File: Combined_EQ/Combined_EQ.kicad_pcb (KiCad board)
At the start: 2 copper layers, 152.3 x 105 mm, 1 part, among them J1 EDA 306

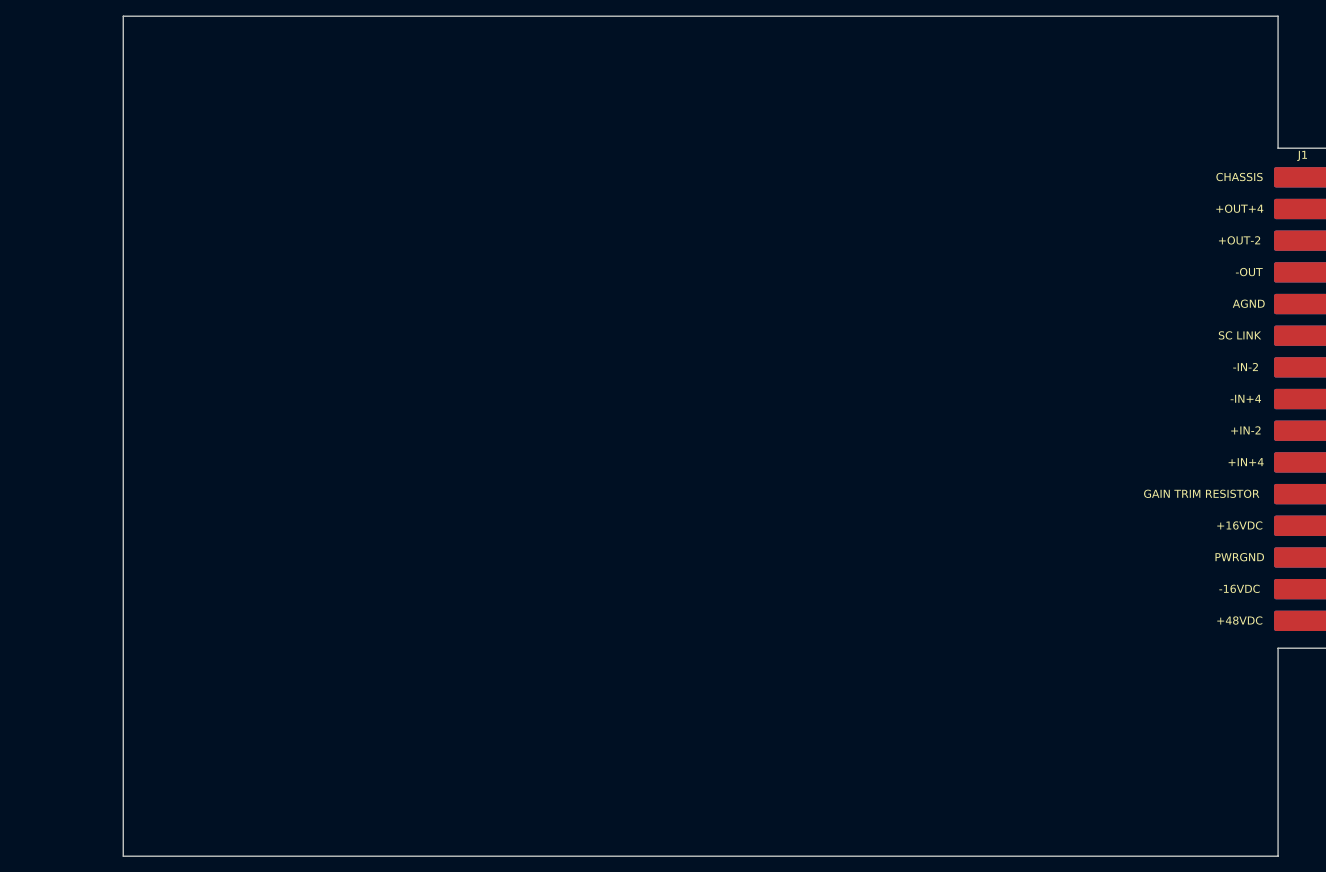
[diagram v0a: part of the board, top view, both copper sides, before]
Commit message: started on pcb
need to footprint for the capacitors
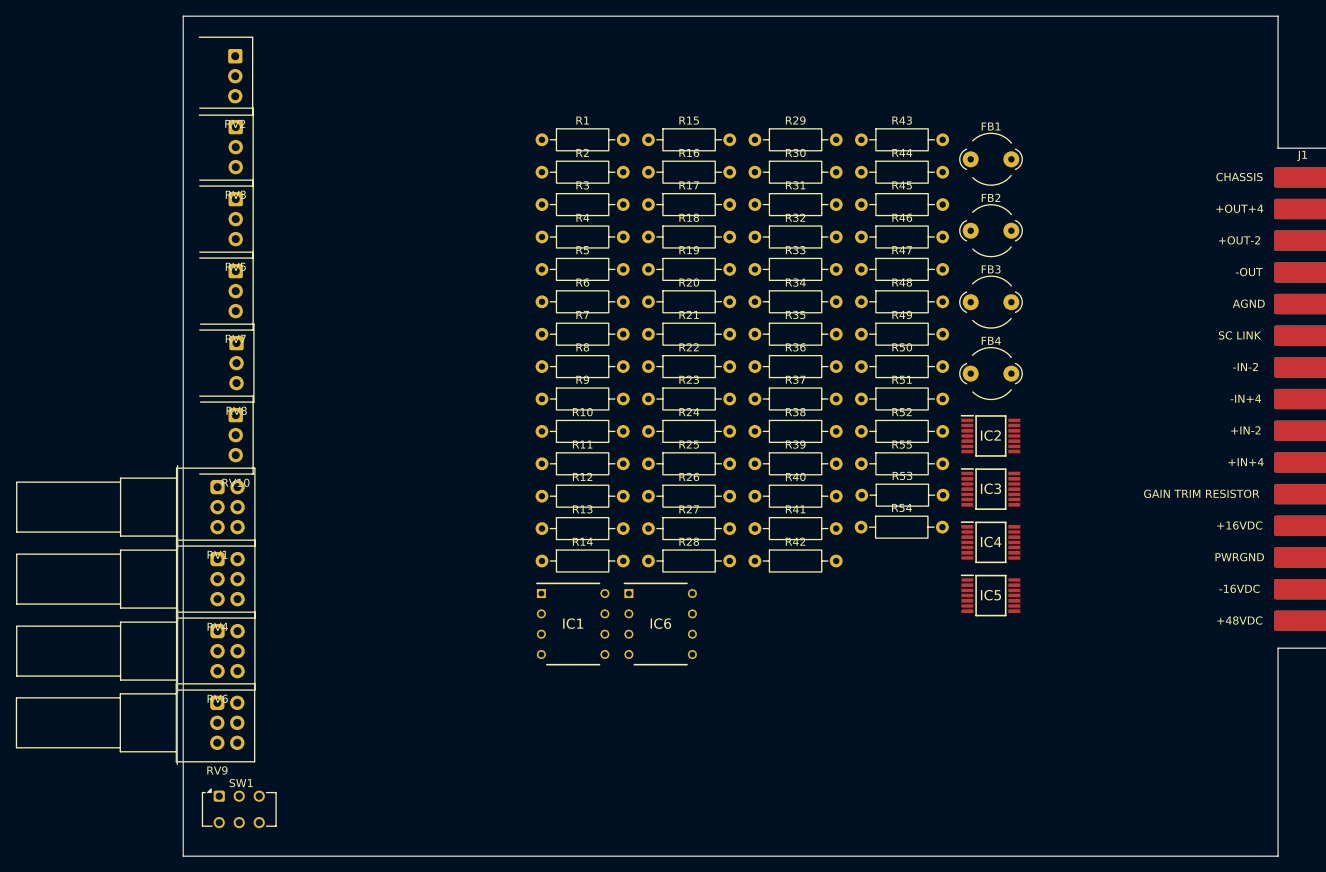
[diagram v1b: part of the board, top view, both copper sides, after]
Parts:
- added FB1: 2944666671, Ferrite_THT:LairdTech_28C0236-0JW-10, F.Cu at (156.6, 72.9)
- added FB2: 2944666671, Ferrite_THT:LairdTech_28C0236-0JW-10, F.Cu at (156.6, 81.8)
- added FB3: 2944666671, Ferrite_THT:LairdTech_28C0236-0JW-10, F.Cu at (156.6, 90.8)
- added FB4: 2944666671, Ferrite_THT:LairdTech_28C0236-0JW-10, F.Cu at (156.6, 99.7)
- added IC1: INA137PA, INA137:DIP794W53P254L959H508Q8N, F.Cu at (106.9, 131.0)
- added IC2: OPA1644AIPWR, OPA1644:SOP65P640X120-14N, F.Cu at (159.1, 107.5)
- added IC3: OPA1644AIPWR, OPA1644:SOP65P640X120-14N, F.Cu at (159.1, 114.1)
- added IC4: OPA1644AIPWR, OPA1644:SOP65P640X120-14N, F.Cu at (159.1, 120.8)
- added IC5: OPA1644AIPWR, OPA1644:SOP65P640X120-14N, F.Cu at (159.1, 127.4)
- added IC6: DRV134PA, INA137:DIP794W53P254L959H508Q8N, F.Cu at (117.8, 131.0)
- added R1: 47, Resistor_THT:R_Axial_DIN0207_L6.3mm_D2.5mm_P10.16mm_Horizontal, F.Cu at (103.0, 70.5)
- added R10: 27K, Resistor_THT:R_Axial_DIN0207_L6.3mm_D2.5mm_P10.16mm_Horizontal, F.Cu at (103.0, 106.9)
- added R11: 16K, Resistor_THT:R_Axial_DIN0207_L6.3mm_D2.5mm_P10.16mm_Horizontal, F.Cu at (103.0, 111.0)
- added R12: 5.6K, Resistor_THT:R_Axial_DIN0207_L6.3mm_D2.5mm_P10.16mm_Horizontal, F.Cu at (103.0, 115.0)
- added R13: 10K, Resistor_THT:R_Axial_DIN0207_L6.3mm_D2.5mm_P10.16mm_Horizontal, F.Cu at (103.0, 119.0)
- added R14: 1k, Resistor_THT:R_Axial_DIN0207_L6.3mm_D2.5mm_P10.16mm_Horizontal, F.Cu at (103.0, 123.1)
- added R15: 3k3, Resistor_THT:R_Axial_DIN0207_L6.3mm_D2.5mm_P10.16mm_Horizontal, F.Cu at (116.3, 70.5)
- added R16: 22k, Resistor_THT:R_Axial_DIN0207_L6.3mm_D2.5mm_P10.16mm_Horizontal, F.Cu at (116.3, 74.5)
- added R17: 22k, Resistor_THT:R_Axial_DIN0207_L6.3mm_D2.5mm_P10.16mm_Horizontal, F.Cu at (116.3, 78.5)
- added R18: 22k, Resistor_THT:R_Axial_DIN0207_L6.3mm_D2.5mm_P10.16mm_Horizontal, F.Cu at (116.3, 82.6)
- added R19: 22k, Resistor_THT:R_Axial_DIN0207_L6.3mm_D2.5mm_P10.16mm_Horizontal, F.Cu at (116.3, 86.7)
- added R2: 100k, Resistor_THT:R_Axial_DIN0207_L6.3mm_D2.5mm_P10.16mm_Horizontal, F.Cu at (103.0, 74.5)
- added R20: 100k, Resistor_THT:R_Axial_DIN0207_L6.3mm_D2.5mm_P10.16mm_Horizontal, F.Cu at (116.3, 90.7)
- added R21: 2k2, Resistor_THT:R_Axial_DIN0207_L6.3mm_D2.5mm_P10.16mm_Horizontal, F.Cu at (116.3, 94.8)
- added R22: 22k, Resistor_THT:R_Axial_DIN0207_L6.3mm_D2.5mm_P10.16mm_Horizontal, F.Cu at (116.3, 98.8)
- added R23: 22k, Resistor_THT:R_Axial_DIN0207_L6.3mm_D2.5mm_P10.16mm_Horizontal, F.Cu at (116.3, 102.8)
- added R24: 10k, Resistor_THT:R_Axial_DIN0207_L6.3mm_D2.5mm_P10.16mm_Horizontal, F.Cu at (116.3, 106.9)
- added R25: 2k2, Resistor_THT:R_Axial_DIN0207_L6.3mm_D2.5mm_P10.16mm_Horizontal, F.Cu at (116.3, 111.0)
- added R26: 10k, Resistor_THT:R_Axial_DIN0207_L6.3mm_D2.5mm_P10.16mm_Horizontal, F.Cu at (116.3, 115.0)
- added R27: 1k, Resistor_THT:R_Axial_DIN0207_L6.3mm_D2.5mm_P10.16mm_Horizontal, F.Cu at (116.3, 119.0)
- added R28: 3k3, Resistor_THT:R_Axial_DIN0207_L6.3mm_D2.5mm_P10.16mm_Horizontal, F.Cu at (116.3, 123.1)
- added R29: 22k, Resistor_THT:R_Axial_DIN0207_L6.3mm_D2.5mm_P10.16mm_Horizontal, F.Cu at (129.6, 70.5)
- added R3: 47, Resistor_THT:R_Axial_DIN0207_L6.3mm_D2.5mm_P10.16mm_Horizontal, F.Cu at (103.0, 78.5)
- added R30: 22k, Resistor_THT:R_Axial_DIN0207_L6.3mm_D2.5mm_P10.16mm_Horizontal, F.Cu at (129.6, 74.5)
- added R31: 22k, Resistor_THT:R_Axial_DIN0207_L6.3mm_D2.5mm_P10.16mm_Horizontal, F.Cu at (129.6, 78.5)
- added R32: 22k, Resistor_THT:R_Axial_DIN0207_L6.3mm_D2.5mm_P10.16mm_Horizontal, F.Cu at (129.6, 82.6)
- added R33: 100k, Resistor_THT:R_Axial_DIN0207_L6.3mm_D2.5mm_P10.16mm_Horizontal, F.Cu at (129.6, 86.7)
- added R34: 2k2, Resistor_THT:R_Axial_DIN0207_L6.3mm_D2.5mm_P10.16mm_Horizontal, F.Cu at (129.6, 90.7)
- added R35: 22k, Resistor_THT:R_Axial_DIN0207_L6.3mm_D2.5mm_P10.16mm_Horizontal, F.Cu at (129.6, 94.8)
- added R36: 10k, Resistor_THT:R_Axial_DIN0207_L6.3mm_D2.5mm_P10.16mm_Horizontal, F.Cu at (129.6, 98.8)
- added R37: 2k2, Resistor_THT:R_Axial_DIN0207_L6.3mm_D2.5mm_P10.16mm_Horizontal, F.Cu at (129.6, 102.8)
- added R38: 10k, Resistor_THT:R_Axial_DIN0207_L6.3mm_D2.5mm_P10.16mm_Horizontal, F.Cu at (129.6, 106.9)
- added R39: 22k, Resistor_THT:R_Axial_DIN0207_L6.3mm_D2.5mm_P10.16mm_Horizontal, F.Cu at (129.6, 111.0)
- added R4: 100k, Resistor_THT:R_Axial_DIN0207_L6.3mm_D2.5mm_P10.16mm_Horizontal, F.Cu at (103.0, 82.6)
- added R40: 30K, Resistor_THT:R_Axial_DIN0207_L6.3mm_D2.5mm_P10.16mm_Horizontal, F.Cu at (129.6, 115.0)
- added R41: 27K, Resistor_THT:R_Axial_DIN0207_L6.3mm_D2.5mm_P10.16mm_Horizontal, F.Cu at (129.6, 119.0)
- added R42: 30K, Resistor_THT:R_Axial_DIN0207_L6.3mm_D2.5mm_P10.16mm_Horizontal, F.Cu at (129.6, 123.1)
- added R43: 16K, Resistor_THT:R_Axial_DIN0207_L6.3mm_D2.5mm_P10.16mm_Horizontal, F.Cu at (142.9, 70.5)
- added R44: 10K, Resistor_THT:R_Axial_DIN0207_L6.3mm_D2.5mm_P10.16mm_Horizontal, F.Cu at (142.9, 74.5)
- added R45: 4.7K, Resistor_THT:R_Axial_DIN0207_L6.3mm_D2.5mm_P10.16mm_Horizontal, F.Cu at (142.9, 78.5)
- added R46: 4.7K, Resistor_THT:R_Axial_DIN0207_L6.3mm_D2.5mm_P10.16mm_Horizontal, F.Cu at (142.9, 82.6)
- added R47: 4.7K, Resistor_THT:R_Axial_DIN0207_L6.3mm_D2.5mm_P10.16mm_Horizontal, F.Cu at (142.9, 86.7)
- added R48: 4.7K, Resistor_THT:R_Axial_DIN0207_L6.3mm_D2.5mm_P10.16mm_Horizontal, F.Cu at (142.9, 90.7)
- added R49: 10K, Resistor_THT:R_Axial_DIN0207_L6.3mm_D2.5mm_P10.16mm_Horizontal, F.Cu at (142.9, 94.8)
- added R5: 10, Resistor_THT:R_Axial_DIN0207_L6.3mm_D2.5mm_P10.16mm_Horizontal, F.Cu at (103.0, 86.7)
- added R50: 10K, Resistor_THT:R_Axial_DIN0207_L6.3mm_D2.5mm_P10.16mm_Horizontal, F.Cu at (142.9, 98.8)
- added R51: 16K, Resistor_THT:R_Axial_DIN0207_L6.3mm_D2.5mm_P10.16mm_Horizontal, F.Cu at (142.9, 102.8)
- added R52: 16K, Resistor_THT:R_Axial_DIN0207_L6.3mm_D2.5mm_P10.16mm_Horizontal, F.Cu at (142.9, 106.9)
- added R53: 16K, Resistor_THT:R_Axial_DIN0207_L6.3mm_D2.5mm_P10.16mm_Horizontal, F.Cu at (143.0, 114.9)
- added R54: 16K, Resistor_THT:R_Axial_DIN0207_L6.3mm_D2.5mm_P10.16mm_Horizontal, F.Cu at (142.9, 118.9)
- added R55: 10K, Resistor_THT:R_Axial_DIN0207_L6.3mm_D2.5mm_P10.16mm_Horizontal, F.Cu at (142.9, 111.0)
- added R6: 10, Resistor_THT:R_Axial_DIN0207_L6.3mm_D2.5mm_P10.16mm_Horizontal, F.Cu at (103.0, 90.7)
- added R7: 100k, Resistor_THT:R_Axial_DIN0207_L6.3mm_D2.5mm_P10.16mm_Horizontal, F.Cu at (103.0, 94.8)
- added R8: 6.2K, Resistor_THT:R_Axial_DIN0207_L6.3mm_D2.5mm_P10.16mm_Horizontal, F.Cu at (103.0, 98.8)
- added R9: 6.2K, Resistor_THT:R_Axial_DIN0207_L6.3mm_D2.5mm_P10.16mm_Horizontal, F.Cu at (103.0, 102.8)
- added RV1: 100K, Potentiometer_THT:Potentiometer_Alps_RK097_Dual_Horizontal, F.Cu at (62.4, 113.9)
- added RV10: 10K, Potentiometer_THT:Potentiometer_Alps_RK097_Single_Horizontal, F.Cu at (64.7, 104.9)
- added RV2: 10k, Potentiometer_THT:Potentiometer_Alps_RK097_Single_Horizontal, F.Cu at (64.7, 60.0)
- added RV3: 10K, Potentiometer_THT:Potentiometer_Alps_RK097_Single_Horizontal, F.Cu at (64.7, 68.9)
- added RV4: 100K, Potentiometer_THT:Potentiometer_Alps_RK097_Dual_Horizontal, F.Cu at (62.4, 122.9)
- added RV5: 10k, Potentiometer_THT:Potentiometer_Alps_RK097_Single_Horizontal, F.Cu at (64.7, 77.9)
- added RV6: 10k, Potentiometer_THT:Potentiometer_Alps_RK097_Dual_Horizontal, F.Cu at (62.4, 131.9)
- added RV7: 10k, Potentiometer_THT:Potentiometer_Alps_RK097_Single_Horizontal, F.Cu at (64.7, 86.9)
- added RV8: 10k, Potentiometer_THT:Potentiometer_Alps_RK097_Single_Horizontal, F.Cu at (64.8, 95.9)
- added RV9: 10k, Potentiometer_THT:Potentiometer_Alps_RK097_Dual_Horizontal, F.Cu at (62.4, 140.8)
- added SW1: SW_Slide_DPDT, Button_Switch_THT:SW_CK_JS202011CQN_DPDT_Straight, F.Cu at (62.6, 152.5)
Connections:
- J1 pad 11: /GAIN_ADJ -> unconnected-(J1-Pin_11-Pad11)
- J1 pad 12: +16V -> VCC
- J1 pad 13: GND -> B+
- J1 pad 14: -16V -> VEE
- J1 pad 15: +48V -> unconnected-(J1-Pin_15-Pad15)
- J1 pad 3: /+OUT-2 -> unconnected-(J1-Pin_3-Pad3)_1
- J1 pad 5: /AGND -> B+
- J1 pad 6: /SC_LINK -> unconnected-(J1-Pin_6-Pad6)
- J1 pad 7: /-IN-2 -> unconnected-(J1-Pin_7-Pad7)
- J1 pad 9: /+IN-2 -> unconnected-(J1-Pin_9-Pad9)
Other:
- board size 152.3 x 105 mm -> 144.8 x 105 mm
- board text removed: "Cut here in case mounted on "L" shaped Aluminium support leaving room for screws form the front panel"
- board text removed: "Cut here in case mounted on "L" shaped aluminium support directly in physical contact with the PCB"
- board text removed: "No room between the PCB and the front panel"

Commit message: half done pcb
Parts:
- added C1: 470p, Capacitor_THT:C_Disc_D5.0mm_W2.5mm_P5.00mm, F.Cu at (186.7, 66.2)
- added C10: 47u, Capacitor_THT:C_Radial_D8.0mm_H7.0mm_P3.50mm, F.Cu at (179.7, 60.0)
- added C11: 1u, Capacitor_THT:C_Disc_D5.0mm_W2.5mm_P5.00mm, F.Cu at (153.2, 57.0)
- added C12: 1u, Capacitor_THT:C_Disc_D5.0mm_W2.5mm_P5.00mm, F.Cu at (157.7, 87.8)
- added C13: 100n, Capacitor_THT:C_Disc_D5.0mm_W2.5mm_P5.00mm, F.Cu at (-20.1, 131.0)
- added C14: 100n, Capacitor_THT:C_Disc_D5.0mm_W2.5mm_P5.00mm, F.Cu at (-20.1, 135.1)
- added C15: 100n, Capacitor_THT:C_Disc_D5.0mm_W2.5mm_P5.00mm, F.Cu at (118.9, 37.0)
- added C16: 100n, Capacitor_THT:C_Disc_D5.0mm_W2.5mm_P5.00mm, F.Cu at (118.9, 41.1)
- added C17: 100n, Capacitor_THT:C_Disc_D5.0mm_W2.5mm_P5.00mm, F.Cu at (227.2, 95.4)
- added C18: 100u, Capacitor_THT:C_Disc_D5.0mm_W2.5mm_P5.00mm, F.Cu at (213.4, 95.0)
- added C19: 100n, Capacitor_THT:C_Disc_D5.0mm_W2.5mm_P5.00mm, F.Cu at (227.2, 99.5)
- added C2: 10u, Capacitor_THT:C_Rect_L4.0mm_W2.5mm_P2.50mm, F.Cu at (-11.2, 115.2)
- added C20: 100u, Capacitor_THT:C_Disc_D5.0mm_W2.5mm_P5.00mm, F.Cu at (213.4, 99.0)
- added C21: 100n, Capacitor_THT:C_Disc_D5.0mm_W2.5mm_P5.00mm, F.Cu at (136.2, 63.5)
- added C22: 100n, Capacitor_THT:C_Disc_D5.0mm_W2.5mm_P5.00mm, F.Cu at (136.2, 86.8)
- added C23: 1u, Capacitor_THT:C_Disc_D5.0mm_W2.5mm_P5.00mm, F.Cu at (-18.1, 107.9)
- added C24: 10n, Capacitor_THT:C_Disc_D5.0mm_W2.5mm_P5.00mm, F.Cu at (120.0, 225.9)
- added C25: 270p, Capacitor_THT:C_Disc_D5.0mm_W2.5mm_P5.00mm, F.Cu at (120.0, 230.0)
- added C26: 270p, Capacitor_THT:C_Disc_D5.0mm_W2.5mm_P5.00mm, F.Cu at (120.0, 234.1)
- added C27: 10n, Capacitor_THT:C_Disc_D5.0mm_W2.5mm_P5.00mm, F.Cu at (120.0, 238.1)
- added C28: 100p, Capacitor_THT:C_Disc_D5.0mm_W2.5mm_P5.00mm, F.Cu at (120.0, 242.2)
- added C29: 220p, Capacitor_THT:C_Disc_D5.0mm_W2.5mm_P5.00mm, F.Cu at (120.0, 246.2)
- added C3: 2.2n, Capacitor_THT:C_Disc_D5.0mm_W2.5mm_P5.00mm, F.Cu at (-20.0, 140.5)
- added C30: 100n, Capacitor_THT:C_Disc_D5.0mm_W2.5mm_P5.00mm, F.Cu at (120.0, 250.2)
- added C31: 100n, Capacitor_THT:C_Disc_D5.0mm_W2.5mm_P5.00mm, F.Cu at (128.2, 221.9)
- added C32: 100n, Capacitor_THT:C_Disc_D5.0mm_W2.5mm_P5.00mm, F.Cu at (229.7, 129.0)
- added C33: 220p, Capacitor_THT:C_Disc_D5.0mm_W2.5mm_P5.00mm, F.Cu at (128.2, 230.0)
- added C34: 100n, Capacitor_THT:C_Disc_D5.0mm_W2.5mm_P5.00mm, F.Cu at (230.4, 134.9)
- added C35: 100p, Capacitor_THT:C_Disc_D5.0mm_W2.5mm_P5.00mm, F.Cu at (230.4, 139.0)
- added C36: 100p, Capacitor_THT:C_Disc_D5.0mm_W2.5mm_P5.00mm, F.Cu at (230.4, 143.0)
- added C37: 100n, Capacitor_THT:C_Disc_D5.0mm_W2.5mm_P5.00mm, F.Cu at (144.9, 57.0)
- added C38: 100n, Capacitor_THT:C_Disc_D5.0mm_W2.5mm_P5.00mm, F.Cu at (157.7, 80.5)
- added C39: 2.2n, Capacitor_THT:C_Disc_D5.0mm_W2.5mm_P5.00mm, F.Cu at (104.4, 19.1)
- added C4: 47u, Capacitor_THT:C_Radial_D8.0mm_H7.0mm_P3.50mm, F.Cu at (179.9, 70.5)
- added C40: 470p, Capacitor_THT:C_Disc_D5.0mm_W2.5mm_P5.00mm, F.Cu at (104.4, 23.1)
- added C41: 100p, Capacitor_THT:C_Disc_D5.0mm_W2.5mm_P5.00mm, F.Cu at (-19.4, 104.2)
- added C42: 2.2n, Capacitor_THT:C_Disc_D5.0mm_W2.5mm_P5.00mm, F.Cu at (104.4, 28.1)
- added C43: 10n, Capacitor_THT:C_Disc_D5.0mm_W2.5mm_P5.00mm, F.Cu at (104.4, 32.1)
- added C44: 100p, Capacitor_THT:C_Disc_D5.0mm_W2.5mm_P5.00mm, F.Cu at (-19.4, 116.4)
- added C46: 10n, Capacitor_THT:C_Disc_D5.0mm_W2.5mm_P5.00mm, F.Cu at (136.3, 246.2)
- added C47: 10n, Capacitor_THT:C_Disc_D5.0mm_W2.5mm_P5.00mm, F.Cu at (136.3, 250.2)
- added C5: 470p, Capacitor_THT:C_Disc_D5.0mm_W2.5mm_P5.00mm, F.Cu at (186.7, 60.8)
- added C6: 2.2n, Capacitor_THT:C_Disc_D5.0mm_W2.5mm_P5.00mm, F.Cu at (-20.0, 145.7)
- added C7: 10u, Capacitor_THT:C_Rect_L4.0mm_W2.5mm_P2.50mm, F.Cu at (102.2, 73.0)
- added C8: 10n, Capacitor_THT:C_Disc_D5.0mm_W2.5mm_P5.00mm, F.Cu at (110.6, 36.8)
- added C9: 470p, Capacitor_THT:C_Disc_D5.0mm_W2.5mm_P5.00mm, F.Cu at (110.6, 40.9)
- added H1: MountingHole, MountingHole:MountingHole_3.2mm_M3, F.Cu at (50.6, 60.0)
- added H2: MountingHole, MountingHole:MountingHole_3.2mm_M3, F.Cu at (73.2, 60.0)
- added H3: MountingHole, MountingHole:MountingHole_3.2mm_M3, F.Cu at (73.2, 155.0)
- added H4: MountingHole, MountingHole:MountingHole_3.2mm_M3, F.Cu at (50.6, 155.0)
- moved IC2 177.1 mm to (-17.3, 123.0)
- moved R15 155.6 mm to (-35.6, 104.0)
- moved R16 155.6 mm to (-35.6, 108.0)
- moved R17 155.6 mm to (-35.6, 112.0)
- moved R18 155.6 mm to (-35.6, 116.1)
- moved R19 155.6 mm to (-35.6, 120.2)
- moved R20 155.6 mm to (-35.6, 124.2)
- moved R21 155.6 mm to (-35.6, 128.2)
- moved R23 154.9 mm to (-35.6, 133.2)
- moved R24 154.9 mm to (-35.6, 137.3)
- moved R25 154.9 mm to (-35.6, 141.3)
- moved R26 154.9 mm to (-35.6, 145.4)
- moved R22 152.3 mm to (-35.9, 95.0)
- moved R14 140.9 mm to (-35.9, 99.5)
- moved SW1 131.7 mm to (179.7, 92.0), turned to -90 degrees
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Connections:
- FB1 pad 2: Net-(FB1-Pad2) -> /-IN
- FB2 pad 2: Net-(FB2-Pad2) -> /+IN
- IC4 pad 4: -16V -> +16V
- R1 pad 1: Net-(FB1-Pad2) -> /-IN
- R3 pad 1: Net-(FB2-Pad2) -> /+IN
- SW1 pad 3: /-IN+4 -> /-IN
- SW1 pad 4: /+IN+4 -> /+IN
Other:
- board size 144.8 x 105 mm -> 167.3 x 105 mm
- copper layers 2 -> 4

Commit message: more progress
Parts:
- moved R38 48.7 mm to (84.6, 89.5), turned to 180 degrees
- moved R37 45.5 mm to (76.8, 81.0)
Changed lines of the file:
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@@
 	(footprint "Resistor_THT:R_Axial_DIN0207_L6.3mm_D2.5mm_P10.16mm_Horizontal"
 		(layer "F.Cu")
-		(at 87.82 40.9)
+		(at 84.56 89.5 180)
 		(descr "Resistor, Axial_DIN0207 series, Axial, Horizontal, pin pitch=10.16mm, 0.25W = 1/4W, length*diameter=6.3*2.5mm^2, http://cdn-reichelt.de/documents/datenblatt/B400/1_4W%23YAG.pdf")
 		(tags "Resistor Axial_DIN0207 series Axial Horizontal pin pitch 10.16mm 0.25W = 1/4W length 6.3mm diameter 2.5mm")
@@
 		)
 		(property "Field5" ""
-			(at 0 0 0)
+			(at 0 0 180)
 			(unlocked yes)
 			(layer "F.Fab")
@@
 		(attr through_hole)
 		(fp_line
-			(start 1.04 0)
-			(end 1.81 0)
+			(start 9.12 0)
+			(end 8.35 0)
 			(stroke
 				(width 0.12)
@@
 		)
 		(fp_line
-			(start 9.12 0)
-			(end 8.35 0)
+			(start 1.04 0)
+			(end 1.81 0)
 			(stroke
 				(width 0.12)
@@
 		)
 		(fp_line
-			(start 0 0)
-			(end 1.93 0)
+			(start 10.16 0)
+			(end 8.23 0)
 			(stroke
 				(width 0.1)
@@
 		)
 		(fp_line
-			(start 10.16 0)
-			(end 8.23 0)
+			(start 0 0)
+			(end 1.93 0)
 			(stroke
 				(width 0.1)
@@
 		)
 		(pad "1" thru_hole circle
-			(at 0 0)
+			(at 0 0 180)
 			(size 1.6 1.6)
 			(drill 0.8)
@@
 		)
 		(pad "2" thru_hole circle
-			(at 10.16 0)
+			(at 10.16 0 180)
 			(size 1.6 1.6)
 			(drill 0.8)
@@
 	(footprint "Resistor_THT:R_Axial_DIN0207_L6.3mm_D2.5mm_P10.16mm_Horizontal"
 		(layer "F.Cu")
-		(at 87.82 36.85)
+		(at 76.82 81)
 		(descr "Resistor, Axial_DIN0207 series, Axial, Horizontal, pin pitch=10.16mm, 0.25W = 1/4W, length*diameter=6.3*2.5mm^2, http://cdn-reichelt.de/documents/datenblatt/B400/1_4W%23YAG.pdf")
 		(tags "Resistor Axial_DIN0207 series Axial Horizontal pin pitch 10.16mm 0.25W = 1/4W length 6.3mm diameter 2.5mm")

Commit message: components placed
need to wire up
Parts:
- removed IC5: OPA1644AIPWR, OPA1644:SOP65P640X120-14N
- added C45: 100n, Capacitor_THT:C_Disc_D5.0mm_W2.5mm_P5.00mm, F.Cu at (127.2, 80.2)
- added C48: 100n, Capacitor_THT:C_Disc_D5.0mm_W2.5mm_P5.00mm, F.Cu at (124.7, 65.0)
- added G***: LOGO, Sound_waves:Sound_Waves, F.Cu at (156.2, 149.5)
- added IC8: OPA1644AID, OPA1644AID:SOIC127P600X175-14N, F.Cu at (145.1, 112.5)
- added J2: Conn_01x17_Pin, Connector_PinHeader_2.54mm:PinHeader_1x17_P2.54mm_Vertical, F.Cu at (56.1, 128.0)
- added J3: Conn_01x17_Pin, Connector_PinSocket_2.54mm:PinSocket_1x17_P2.54mm_Vertical, F.Cu at (80.8, 102.8)
- added U1: OPA1641, OPA1641AID:SOIC127P600X175-8N, F.Cu at (127.2, 70.8)
- IC2, IC3, IC4: value OPA1644AIPWR -> OPA1644AID; footprint OPA1644:SOP65P640X120-14N -> OPA1644AID:SOIC127P600X175-14N
- moved C47 194.5 mm to (52.9, 74.5), turned to 90 degrees
- moved C46 192.7 mm to (48.9, 74.5), turned to 90 degrees
- moved C27 172.9 mm to (52.4, 79.0), turned to 180 degrees
- moved C24 157.3 mm to (52.4, 84.0), turned to 180 degrees
- moved R9 154.5 mm to (38.6, 66.0)
- moved C28 140.7 mm to (150.2, 104.8)
- moved R24 137.8 mm to (101.1, 155.1)
- moved R42 137.3 mm to (47.3, 121.4), turned to -90 degrees
- moved R20 136.2 mm to (100.2, 135.2), turned to 90 degrees
- moved C41 136.0 mm to (108.7, 150.1), turned to 90 degrees
- moved R18 131.9 mm to (90.7, 154.2), turned to 180 degrees
- moved R7 129.2 mm to (105.7, 120.4), turned to -90 degrees
- moved R40 128.5 mm to (51.6, 121.4), turned to -90 degrees
- moved C30 128.4 mm to (145.9, 124.5), turned to 90 degrees
- moved R26 126.2 mm to (90.2, 134.9), turned to 90 degrees
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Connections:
- C13 pad 2: -16V -> +16V
- C24 pad 1: Ko -> /T14
- C25 pad 2: Net-(C25-Pad2) -> /B2
- C26 pad 1: Net-(C25-Pad2) -> /B2
- C27 pad 1: Ko -> /T14
- C30 pad 2: -16V -> +16V
- C46 pad 1: K+ -> /T12
- C46 pad 2: B+ -> /T15
- C47 pad 1: K+ -> /T12
- C47 pad 2: B+ -> /T15
- IC1 pad 5: I+ -> Net-(IC1-OUTPUT)
- IC1 pad 6: I+ -> Net-(IC1-OUTPUT)
- IC2 pad 4: -16V -> +16V
- IC4 pad 1: I- -> unconnected-(IC4-OUT_A-Pad1)
- IC4 pad 2: I- -> unconnected-(IC4--IN_A-Pad2)
- IC4 pad 3: I+ -> unconnected-(IC4-+_IN_A-Pad3)
- R21 pad 2: B+ -> /T15
- R24 pad 2: Net-(R24-Pad2) -> /B7
- R25 pad 2: B+ -> /T15
- R26 pad 2: Net-(R26-Pad2) -> /B4
- R29 pad 1: I- -> Net-(U1--)
- R34 pad 2: B+ -> /T15
- R36 pad 2: Net-(R36-Pad2) -> /B10
- R37 pad 2: B+ -> /T15
- R38 pad 2: Net-(R38-Pad2) -> /B8
- R40 pad 1: Net-(C25-Pad2) -> /T2
- R42 pad 1: L+ -> /T3
- R8 pad 2: Net-(R8-Pad2) -> /B13
- RV1 pad 1: Net-(R8-Pad2) -> /T13
- RV1 pad 2: Net-(R8-Pad2) -> /T13
- RV1 pad 6: K+ -> /T12
- RV4 pad 3: B+ -> /T15
- RV4 pad 6: Lo -> /T1
- RV6 pad 1: Eo -> /T6
- RV6 pad 2: Net-(R24-Pad2) -> /T7
- RV6 pad 4: Fo -> /T5
- RV6 pad 5: Net-(R26-Pad2) -> /T4
- RV8 pad 1: I- -> Net-(U1--)
- RV9 pad 1: Ao -> /T11
- RV9 pad 2: Net-(R36-Pad2) -> /T10
- RV9 pad 4: Bo -> /T9
- RV9 pad 5: Net-(R38-Pad2) -> /T8
